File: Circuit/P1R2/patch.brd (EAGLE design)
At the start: 50.8 x 50.8 mm, 65 parts, among them U1 MK20DX256VLH7, U2 TPS61200, U3 MPU-9250, Y1 32.768KHz, Y2 16Mhz/8pF, Y3 26 Mhz, Y4 16 Mhz

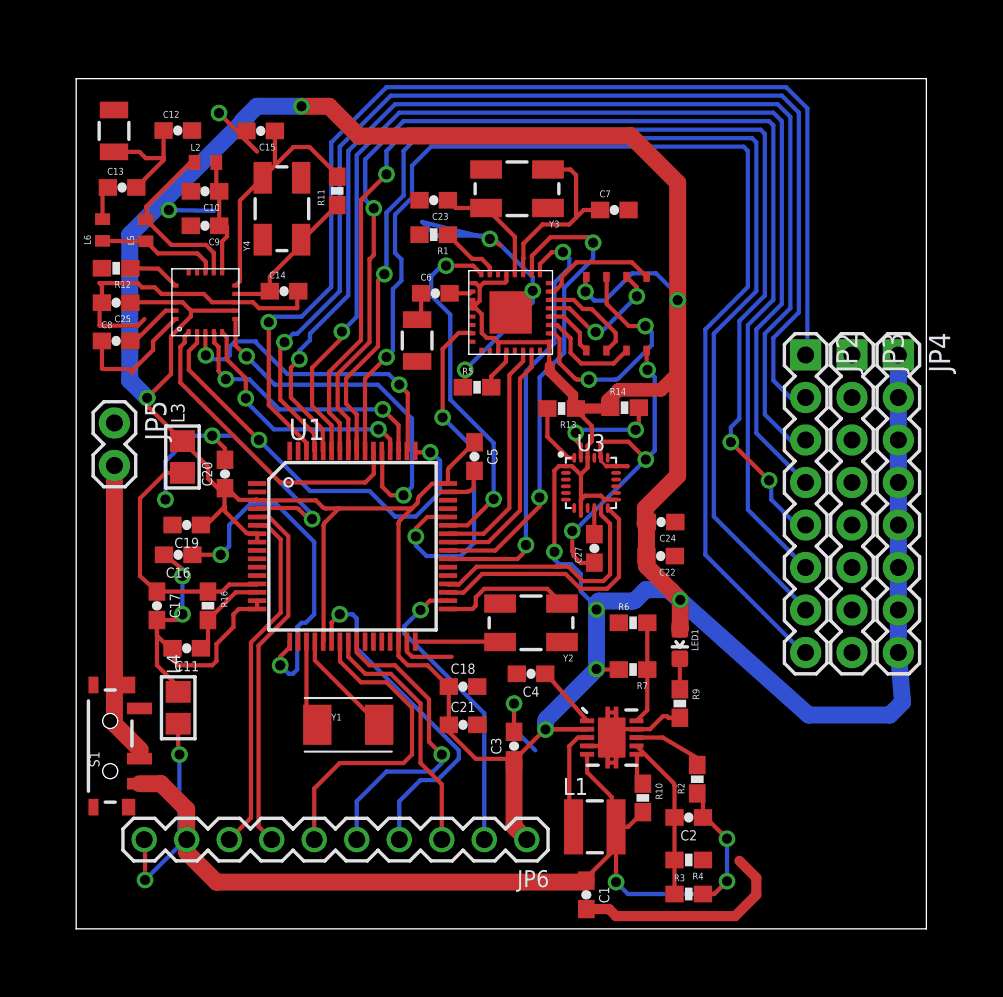
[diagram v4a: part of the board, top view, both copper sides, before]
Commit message: LEDs and GPIO finished. Rough R2 board done
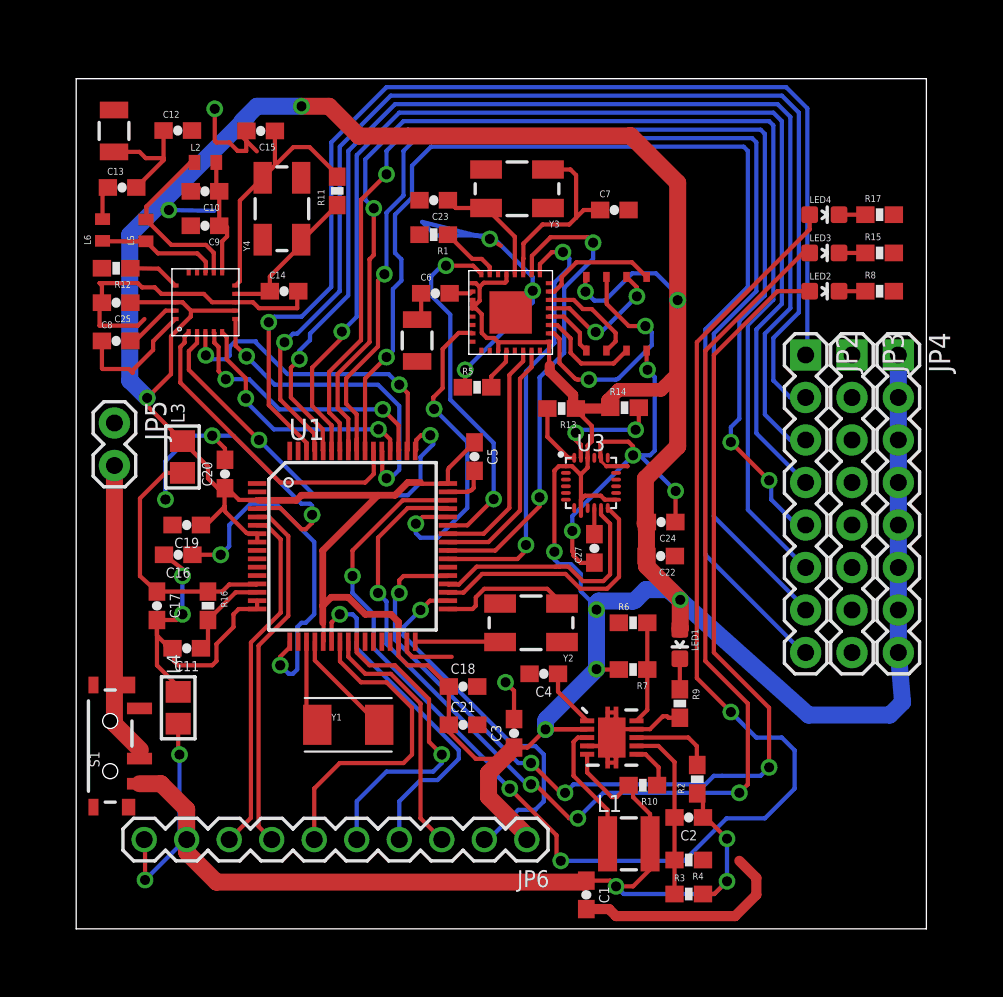
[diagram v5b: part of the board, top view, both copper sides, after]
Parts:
- added LED2, LED3, LED4: (no value), appfruits:LED-0603
- added R15, R17, R8: 330, appfruits:0603-RES
- moved L1 2.27 mm to (33.0, 5.08)
- moved C4 0.76 mm to (27.9, 15.2)
- moved R10 0.76 mm to (33.9, 8.59), turned to 180 degrees
- moved C3 0.76 mm to (26.2, 11.7)
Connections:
- new net N$7: LED2.C, R8.1
- new net N$8: LED3.C, R15.1
- new net N$9: LED4.C, R17.1
- net GND: now also R15.2, R17.2, R8.2
- net PTB2: now also LED2.A
- net PTC2: now also LED3.A
- net PTC3: now also LED4.A
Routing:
- net PTC3: track 0.00 -> 86.8 mm, vias 0 -> 4
- net PTC2: track 0.00 -> 73.8 mm, vias 0 -> 4
- net PTB2: track 0.00 -> 66.8 mm, vias 0 -> 4
- net GND: track 149.4 -> 155.7 mm, vias 14 -> 15
- net RESET_B: track 18.0 -> 22.4 mm
- net PTC8: track 22.4 -> 19.4 mm
- net PTC1: track 21.8 -> 19.3 mm
- net 3.3V: track 245.2 -> 247.3 mm
- net N$2: track 6.21 -> 7.85 mm
- net N$9: track 0.00 -> 1.57 mm
- net N$8: track 0.00 -> 1.57 mm
- net N$7: track 0.00 -> 1.57 mm
- net VCC: track 59.1 -> 60.2 mm
- net PS: track 4.38 -> 5.38 mm
- net SOFTPOWER: track 1.93 -> 2.75 mm
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
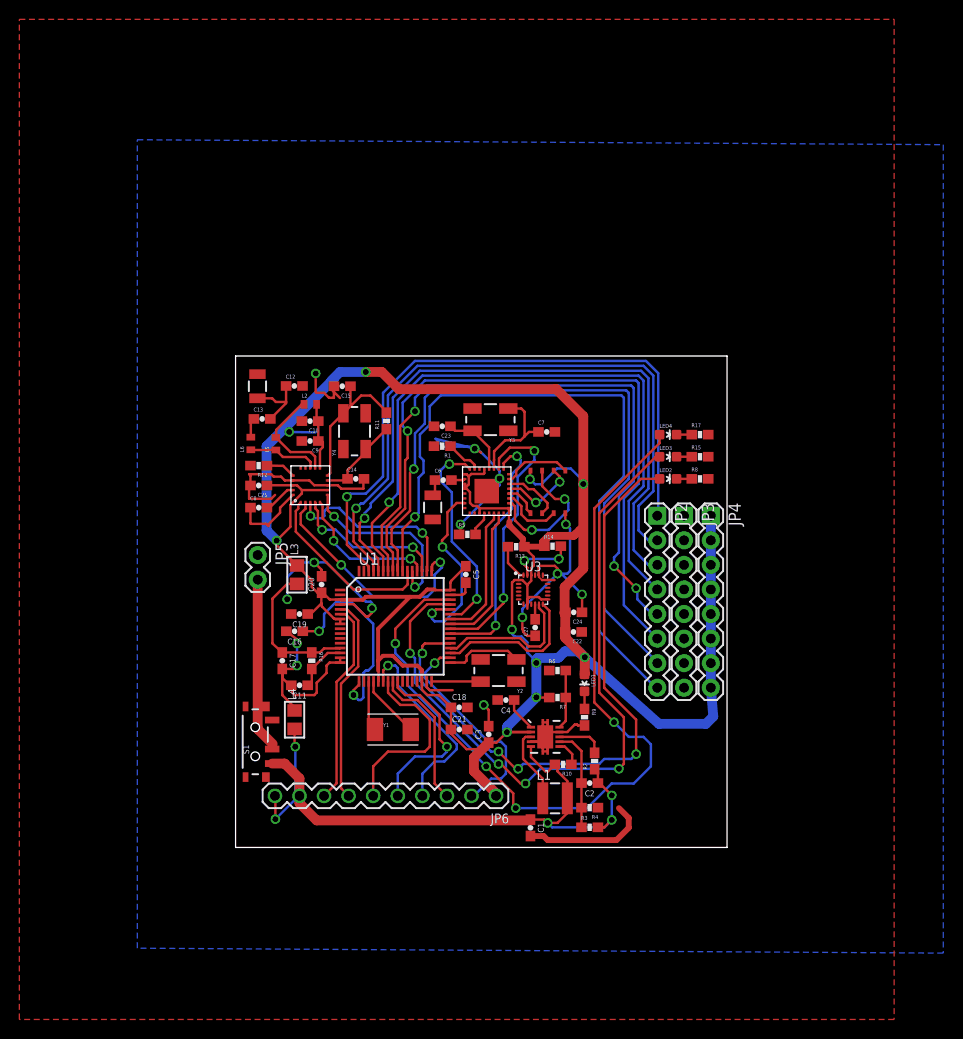
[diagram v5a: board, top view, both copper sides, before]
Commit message: Last couple power connections left. Everything else is placed
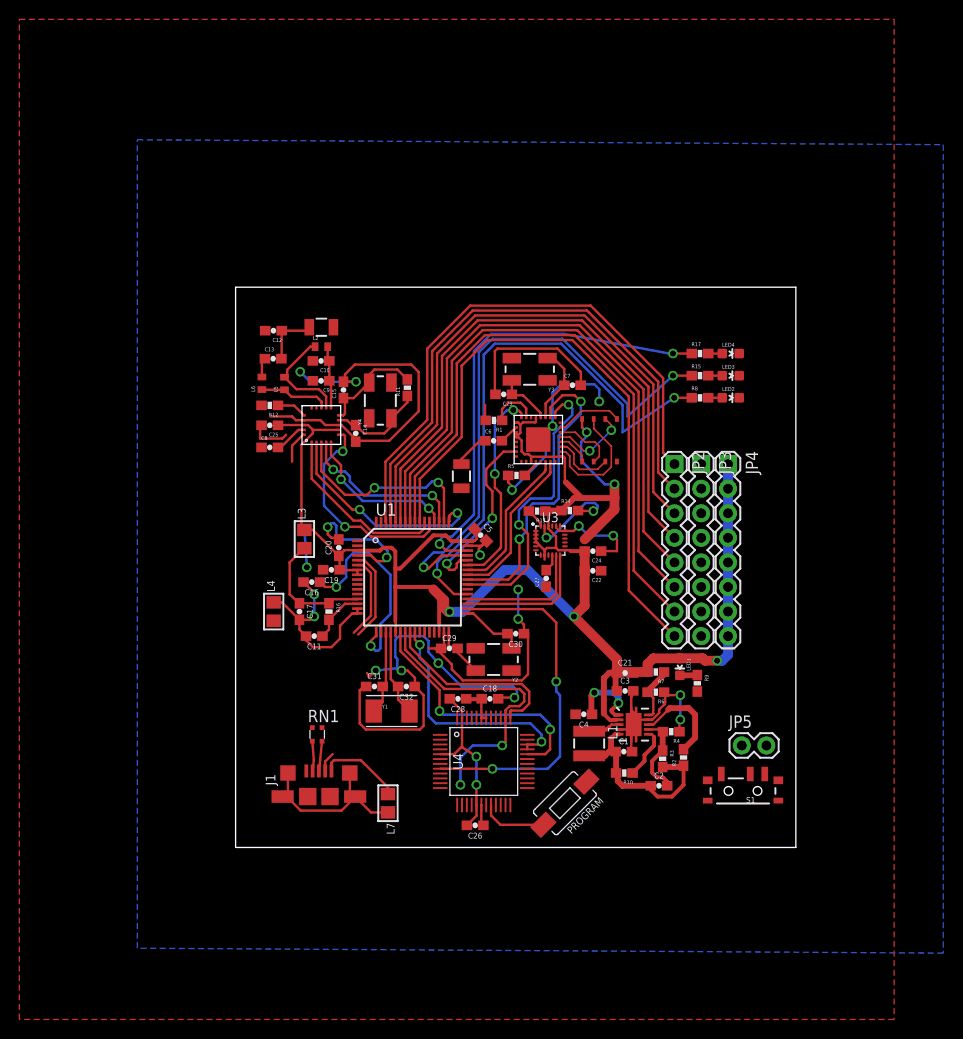
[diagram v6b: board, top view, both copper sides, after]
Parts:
- removed JP6: M100.1, umich:1X10
- added C26, C28: 0.1uF, appfruits:0603-CAP
- added C29, C30, C31, C32: 22 pF, appfruits:0603-CAP
- added J1: 1981584-1, con-usb:1981584-1
- added L7: 600 Ohm/100 Mhz, appfruits:0805
- added PROGRAM: Program, SparkFun-Electromechanical:TACTILE-SWITCH-1101NE
- added RN1: 33, resistor-dil:EXB34V
- added U4: MINI54TAN, TeensyCustom:MINI54TAN
- moved JP5 53.8 mm to (52.3, 10.5), turned to 0 degrees
- moved S1 50.7 mm to (52.5, 5.84), turned to 180 degrees
- moved C21 18.1 mm to (40.3, 18.0)
- moved C3 14.8 mm to (40.3, 16.2), turned to 0 degrees
- moved C1 12.5 mm to (40.1, 9.91), turned to 0 degrees
- moved R9 12.2 mm to (47.7, 17.0)
- moved R4 11.5 mm to (45.0, 12.0)
- moved L4 11.4 mm to (3.94, 24.4)
- moved LED4 10.6 mm to (51.2, 51.1)
- moved LED2 10.6 mm to (51.2, 46.5)
- moved LED3 10.6 mm to (51.2, 48.8)
- moved R7 10.5 mm to (43.4, 18.1)
- moved R6 10.4 mm to (43.4, 16.1), turned to 180 degrees
- moved R3 10.4 mm to (44.1, 9.17), turned to 270 degrees
- moved LED1 9.99 mm to (45.9, 18.7)
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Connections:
- new net N$10: PROGRAM.P$2, U4.20
- new net N$11: C26.1, U4.18
- new net USB_CON_N: J1.2, RN1.1
- new net USB_CON_P: J1.3, RN1.2
- new net USB_SHIELD: J1.S1, J1.S2, J1.S3, J1.S4, L7.2
- net 3.3V: now also C28.1, U4.42, U4.43; no longer JP6.1
- net GND: now also C26.2, C28.2, C29.1, C30.1, C31.1, C32.1, J1.5, L7.1, LED2.C, LED3.C, LED4.C, PROGRAM.P$1, U4.17, U4.25, U4.47, U4.5; no longer JP6.10, R15.2, R17.2, R8.2
- net ID: now also J1.4, U4.38; no longer JP6.6
- net N$27: now also C29.2
- net N$28: now also C30.2
- net N$29: now also C31.2
- net N$30: now also C32.2
- net N$7: now also LED2.A, R8.2; no longer LED2.C, R8.1
- net N$8: now also LED3.A, R15.2; no longer LED3.C, R15.1
- net N$9: now also LED4.A, R17.2; no longer LED4.C, R17.1
- net PTA2: now also U4.37; no longer JP6.3
- net PTB2: now also R8.1; no longer LED2.A
- net PTC2: now also R15.1; no longer LED3.A
- net PTC3: now also R17.1; no longer LED4.A
- net RESET_B: now also U4.8; no longer JP6.2
- net SWD_CLK: now also U4.32; no longer JP6.4
- net SWD_DIO: now also U4.33, U4.34; no longer JP6.5
- net USB_D_N: now also RN1.4; no longer JP6.8
- net USB_D_P: now also RN1.3; no longer JP6.7
- net VCC: now also J1.1; no longer JP6.9
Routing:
- net 3.3V: track 247.3 -> 199.6 mm, vias 10 -> 6
- net VCC: track 60.2 -> 21.7 mm, vias 3 -> 0
- net PTC3: track 86.8 -> 48.6 mm, vias 4 -> 2
- net N$14: track 0.00 -> 20.4 mm
- net USB_SHIELD: track 0.00 -> 18.3 mm
- net VRAW: track 18.2 -> 0.00 mm
- net N$31: track 0.00 -> 16.0 mm
- net PTC2: track 73.8 -> 58.6 mm, vias 4 -> 2
- net N$15: track 0.00 -> 15.1 mm
- net RESET_B: track 22.4 -> 36.7 mm, vias 1 -> 2
- net ID: track 19.2 -> 32.6 mm, vias 0 -> 2
- net USB_D_N: track 21.0 -> 8.65 mm
- net USB_D_P: track 21.5 -> 9.62 mm
- net PTD0: track 73.7 -> 63.4 mm, vias 1 -> 0
- net GND: track 155.7 -> 165.3 mm, vias 15 -> 21
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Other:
- board size 50.8 x 50.8 mm -> 57.9 x 57.9 mm

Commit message: Reversioning, now R1, R2, R3 present
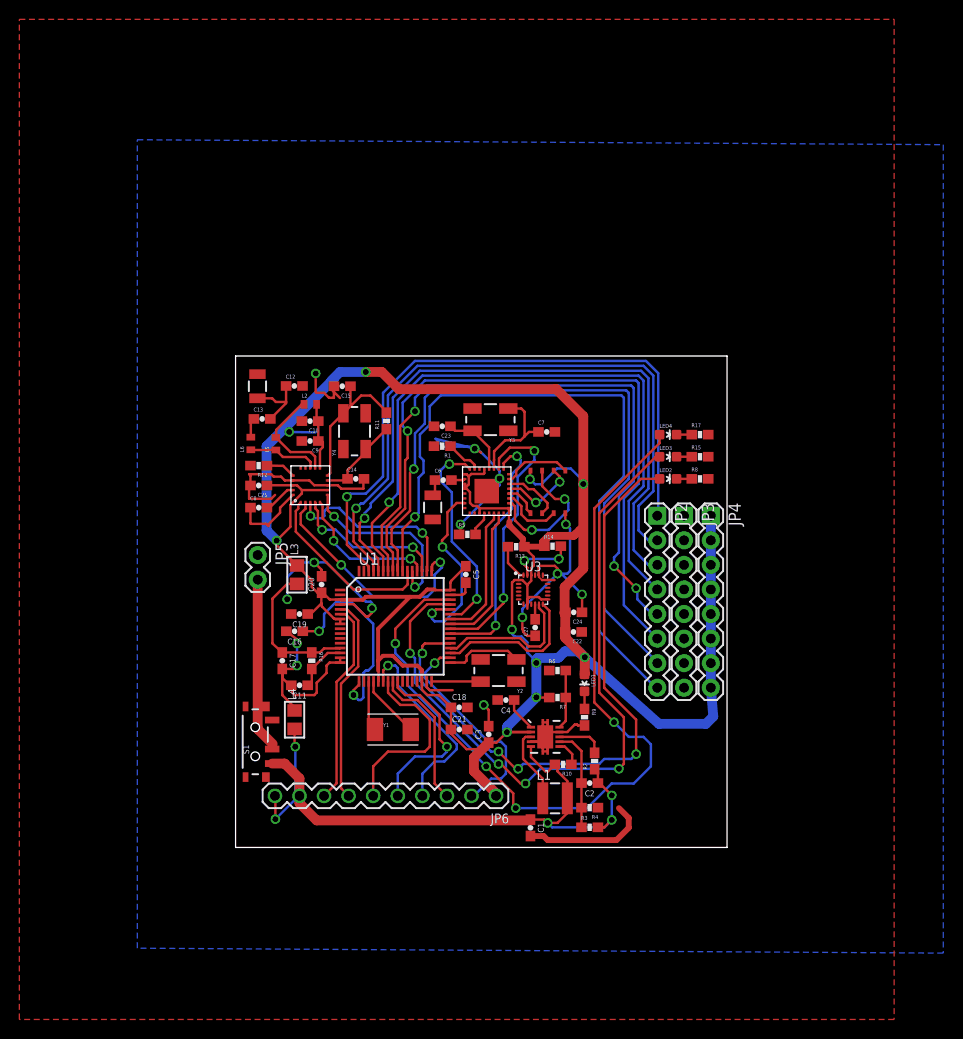
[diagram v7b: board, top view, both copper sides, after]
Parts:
- removed C26, C28: 0.1uF, appfruits:0603-CAP
- removed C29, C30, C31, C32: 22 pF, appfruits:0603-CAP
- removed J1: 1981584-1, con-usb:1981584-1
- removed L7: 600 Ohm/100 Mhz, appfruits:0805
- removed PROGRAM: Program, SparkFun-Electromechanical:TACTILE-SWITCH-1101NE
- removed RN1: 33, resistor-dil:EXB34V
- removed U4: MINI54TAN, TeensyCustom:MINI54TAN
- added JP6: M100.1, umich:1X10
- moved JP5 53.8 mm to (2.29, 30.2), turned to 270 degrees
- moved S1 50.7 mm to (2.03, 10.9), turned to 90 degrees
- moved C21 18.1 mm to (23.1, 12.2)
- moved C3 14.8 mm to (26.2, 11.7), turned to 90 degrees
- moved C1 12.5 mm to (30.5, 2.03), turned to 270 degrees
- moved R9 12.2 mm to (36.1, 13.5)
- moved R4 11.5 mm to (36.6, 4.11)
- moved L4 11.4 mm to (6.10, 13.2)
- moved LED4 10.6 mm to (44.7, 42.7)
- moved LED2 10.6 mm to (44.7, 38.1)
- moved LED3 10.6 mm to (44.7, 40.4)
- moved R7 10.5 mm to (33.3, 15.5)
- moved R6 10.4 mm to (33.3, 18.3), turned to 0 degrees
- moved R3 10.4 mm to (36.6, 2.08), turned to 0 degrees
- moved LED1 9.99 mm to (36.1, 17.0)
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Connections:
- removed net N$10: PROGRAM.P$2, U4.20
- removed net N$11: C26.1, U4.18
- removed net USB_CON_N: J1.2, RN1.1
- removed net USB_CON_P: J1.3, RN1.2
- removed net USB_SHIELD: J1.S1, J1.S2, J1.S3, J1.S4, L7.2
- net 3.3V: now also JP6.1; no longer C28.1, U4.42, U4.43
- net GND: now also JP6.10, R15.2, R17.2, R8.2; no longer C26.2, C28.2, C29.1, C30.1, C31.1, C32.1, J1.5, L7.1, LED2.C, LED3.C, LED4.C, PROGRAM.P$1, U4.17, U4.25, U4.47, U4.5
- net ID: now also JP6.6; no longer J1.4, U4.38
- net N$27: no longer C29.2
- net N$28: no longer C30.2
- net N$29: no longer C31.2
- net N$30: no longer C32.2
- net N$7: now also LED2.C, R8.1; no longer LED2.A, R8.2
- net N$8: now also LED3.C, R15.1; no longer LED3.A, R15.2
- net N$9: now also LED4.C, R17.1; no longer LED4.A, R17.2
- net PTA2: now also JP6.3; no longer U4.37
- net PTB2: now also LED2.A; no longer R8.1
- net PTC2: now also LED3.A; no longer R15.1
- net PTC3: now also LED4.A; no longer R17.1
- net RESET_B: now also JP6.2; no longer U4.8
- net SWD_CLK: now also JP6.4; no longer U4.32
- net SWD_DIO: now also JP6.5; no longer U4.33, U4.34
- net USB_D_N: now also JP6.8; no longer RN1.4
- net USB_D_P: now also JP6.7; no longer RN1.3
- net VCC: now also JP6.9; no longer J1.1
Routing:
- net 3.3V: track 199.6 -> 247.3 mm, vias 6 -> 10
- net VCC: track 21.7 -> 60.2 mm, vias 0 -> 3
- net PTC3: track 48.6 -> 86.8 mm, vias 2 -> 4
- net N$14: track 20.4 -> 0.00 mm
- net USB_SHIELD: track 18.3 -> 0.00 mm
- net VRAW: track 0.00 -> 18.2 mm
- net N$31: track 16.0 -> 0.00 mm
- net PTC2: track 58.6 -> 73.8 mm, vias 2 -> 4
- net N$15: track 15.1 -> 0.00 mm
- net RESET_B: track 36.7 -> 22.4 mm, vias 2 -> 1
- net ID: track 32.6 -> 19.2 mm, vias 2 -> 0
- net USB_D_N: track 8.65 -> 21.0 mm
- net USB_D_P: track 9.62 -> 21.5 mm
- net PTD0: track 63.4 -> 73.7 mm, vias 0 -> 1
- net GND: track 165.3 -> 155.7 mm, vias 21 -> 15
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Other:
- board size 57.9 x 57.9 mm -> 50.8 x 50.8 mm
